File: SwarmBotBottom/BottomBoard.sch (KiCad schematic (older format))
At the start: 19 parts, among them J1 Conn_01x04_Male, J2 Conn_01x04_Male, J6 Conn_01x08_Female, U4 MCP73831-2-OT

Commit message: Camera routing with all sensors and motors
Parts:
- removed D1: LED, LED_SMD:LED_0603_1608Metric, symbol Device:LED
- removed JP1: Jumper_NO_Small, Jumper:SolderJumper-2_P1.3mm_Open_Pad1.0x1.5mm, symbol Device:Jumper_NO_Small
- removed R16, R17: R, Resistor_SMD:R_0402_1005Metric, symbol Device:R
- added C7, C8, C9: C, Capacitor_SMD:C_0402_1005Metric, symbol Device:C
- added D3: LED, LED_SMD:LED_0603_1608Metric, symbol Device:LED
- added IC1: VEML6040A3OG, VEML6040A3OG:VEML6040A3OG, symbol VEML6040A3OG:VEML6040A3OG
- added J3: Conn_01x02_Male, Connector_PinHeader_2.54mm:PinHeader_1x02_P2.54mm_Vertical_SMD_Pin1Left, symbol Connector:Conn_01x02_Male
- added R21: R, Resistor_SMD:R_0402_1005Metric, symbol Device:R
- added U3: MIC5366-3.3YC5, Package_TO_SOT_SMD:SOT-353_SC-70-5, symbol Regulator_Linear:MIC5366-3.3YC5
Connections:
- net labels added: +3.3V, SCL, SDA
- wire segments 8 -> 7
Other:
- moved on the sheet: C20, C21, D2, R15, R18, U4

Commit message: things
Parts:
- added C10: C, Capacitor_SMD:C_0402_1005Metric, symbol Device:C
- added D1, D4, D5: LED, LED_SMD:LED_0603_1608Metric, symbol Device:LED
- added IC2: PCA9570GMH, PCA9570GMH:PCA9570GMH, symbol PCA9570GMH:PCA9570GMH
- added R16, R17, R22: R, Resistor_SMD:R_0402_1005Metric, symbol Device:R
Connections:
- net +3V3: now also C10.1, IC2.8 (VDD)
- net +BATT: no longer R21.2
- net GND: now also C10.2, D1.1 (K), D4.1 (K), D5.1 (K), IC2.4 (VSS)
- net SCL: now also IC2.6 (SCL)
- net SDA: now also IC2.7 (SDA)
- new net: D4.2 (A), R17.1
- new net: D5.2 (A), R22.1
- new net: D1.2 (A), R16.1
- new net IRLED: IC2.5 (P3), R16.2
- new net POWERLED: IC2.2 (P1), R17.2
- new net UVLED: IC2.3 (P2), R22.2
- new net WHITELED: IC2.1 (P0), R21.2
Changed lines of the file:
@@
-$EndComp
-$Comp
-L power:+BATT #PWR0141
-U 1 1 5DF974D8
-P 9700 3400
-F 0 "#PWR0141" H 9700 3250 50  0001 C CNN
-F 1 "+BATT" V 9715 3527 50  0000 L CNN
-F 2 "" H 9700 3400 50  0001 C CNN
-F 3 "" H 9700 3400 50  0001 C CNN
-	1    9700 3400
-	0    -1   -1   0
 $EndComp
 $Comp
@@
 Wire Wire Line
 	700  6900 700  7300
+$Comp
+L PCA9570GMH:PCA9570GMH IC2
+U 1 1 5DFDA85C
+P 7750 5150
+F 0 "IC2" H 8250 5415 50  0000 C CNN
+F 1 "PCA9570GMH" H 8250 5324 50  0000 C CNN
+F 2 "PCA9570GMH:PCA9570GMH" H 8600 5250 50  0001 L CNN
+F 3 "https://www.nxp.com/docs/en/data-sheet/PCA9570.pdf" H 8600 5150 50  0001 L CNN
+F 4 "NXP - PCA9570GMH - I/O EXPANDER, 4BIT, 400KHZ, XQFN-8" H 8600 5050 50  0001 L CNN "Description"
+F 5 "" H 8600 4950 50  0001 L CNN "Height"
+F 6 "Nexperia" H 8600 4850 50  0001 L CNN "Manufacturer_Name"
+F 7 "PCA9570GMH" H 8600 4750 50  0001 L CNN "Manufacturer_Part_Number"
+F 8 "771-PCA9570GMH" H 8600 4650 50  0001 L CNN "Mouser Part Number"
+F 9 "https://www.mouser.com/Search/Refine.aspx?Keyword=771-PCA9570GMH" H 8600 4550 50  0001 L CNN "Mouser Price/Stock"
+F 10 "" H 8600 4450 50  0001 L CNN "RS Part Number"
+F 11 "" H 8600 4350 50  0001 L CNN "RS Price/Stock"
+	1    7750 5150
+	1    0    0    -1
+$EndComp
+Text Label 8750 5350 0    50   ~ 0
+SDA
+Text Label 8750 5250 0    50   ~ 0
+SCL
+$Comp
+L power:GND #PWR0141
+U 1 1 5DFDB907
+P 7750 5450
+F 0 "#PWR0141" H 7750 5200 50  0001 C CNN
+F 1 "GND" V 7755 5322 50  0000 R CNN
+F 2 "" H 7750 5450 50  0001 C CNN
+F 3 "" H 7750 5450 50  0001 C CNN
+	1    7750 5450
+	0    1    1    0
+$EndComp
+$Comp
+L Device:C C10
+U 1 1 5DFDBAA0
+P 8750 5600
+F 0 "C10" H 8865 5646 50  0000 L CNN
+F 1 "C" H 8865 5555 50  0000 L CNN
+F 2 "Capacitor_SMD:C_0402_1005Metric" H 8788 5450 50  0001 C CNN
+F 3 "~" H 8750 5600 50  0001 C CNN
+	1    8750 5600
+	1    0    0    -1
+$EndComp
+$Comp
+L power:+3.3V #PWR0143
+U 1 1 5DFDBDF8
+P 8750 5450
+F 0 "#PWR0143" H 8750 5300 50  0001 C CNN
+F 1 "+3.3V" V 8765 5578 50  0000 L CNN
+F 2 "" H 8750 5450 50  0001 C CNN
+F 3 "" H 8750 5450 50  0001 C CNN
+	1    8750 5450
+	0    1    1    0
+$EndComp
+Connection ~ 8750 5450
+$Comp
+L power:GND #PWR0144
+U 1 1 5DFDC25F
+P 8750 5750
+F 0 "#PWR0144" H 8750 5500 50  0001 C CNN
+F 1 "GND" H 8755 5577 50  0000 C CNN
+F 2 "" H 8750 5750 50  0001 C CNN
+F 3 "" H 8750 5750 50  0001 C CNN
+	1    8750 5750
+	1    0    0    -1
+$EndComp
+$Comp
+L Device:LED D4
+U 1 1 5DFDE198
+P 10200 4550
+F 0 "D4" H 10193 4295 50  0000 C CNN
+F 1 "LED" H 10193 4386 50  0000 C CNN
+F 2 "LED_SMD:LED_0603_1608Metric" H 10200 4550 50  0001 C CNN
+F 3 "~" H 10200 4550 50  0001 C CNN
+	1    10200 4550
+	-1   0    0    1
+$EndComp
+$Comp
+L Device:R R17
+U 1 1 5DFDE19E
+P 9900 4550
+F 0 "R17" V 9693 4550 50  0000 C CNN
+F 1 "R" V 9784 4550 50  0000 C CNN
+F 2 "Resistor_SMD:R_0402_1005Metric" V 9830 4550 50  0001 C CNN
+F 3 "~" H 9900 4550 50  0001 C CNN
+	1    9900 4550
+	0    1    1    0
+$EndComp
+$Comp
+L power:GND #PWR0145
+U 1 1 5DFDE1AA
+P 10350 4550
+F 0 "#PWR0145" H 10350 4300 50  0001 C CNN
+F 1 "GND" H 10355 4377 50  0000 C CNN
+F 2 "" H 10350 4550 50  0001 C CNN
+F 3 "" H 10350 4550 50  0001 C CNN
+	1    10350 4550
+	1    0    0    -1
+$EndComp
+$Comp
+L Device:LED D5
+U 1 1 5DFDE8F2
+P 10200 5050
+F 0 "D5" H 10193 4795 50  0000 C CNN
+F 1 "LED" H 10193 4886 50  0000 C CNN
+F 2 "LED_SMD:LED_0603_1608Metric" H 10200 5050 50  0001 C CNN
+F 3 "~" H 10200 5050 50  0001 C CNN
+	1    10200 5050
+	-1   0    0    1
+$EndComp
+$Comp
+L Device:R R22
+U 1 1 5DFDE8F8
+P 9900 5050
+F 0 "R22" V 9693 5050 50  0000 C CNN
+F 1 "R" V 9784 5050 50  0000 C CNN
+F 2 "Resistor_SMD:R_0402_1005Metric" V 9830 5050 50  0001 C CNN
+F 3 "~" H 9900 5050 50  0001 C CNN
+	1    9900 5050
+	0    1    1    0
+$EndComp
+$Comp
+L power:GND #PWR0146
+U 1 1 5DFDE904
+P 10350 5050
+F 0 "#PWR0146" H 10350 4800 50  0001 C CNN
+F 1 "GND" H 10355 4877 50  0000 C CNN
+F 2 "" H 10350 5050 50  0001 C CNN
+F 3 "" H 10350 5050 50  0001 C CNN
+	1    10350 5050
+	1    0    0    -1
+$EndComp
+$Comp
+L Device:LED D1
+U 1 1 5DFDF294
+P 10150 5550
+F 0 "D1" H 10143 5295 50  0000 C CNN
+F 1 "LED" H 10143 5386 50  0000 C CNN
+F 2 "LED_SMD:LED_0603_1608Metric" H 10150 5550 50  0001 C CNN
+F 3 "~" H 10150 5550 50  0001 C CNN
+	1    10150 5550
+	-1   0    0    1
+$EndComp
+$Comp
+L Device:R R16
+U 1 1 5DFDF29A
+P 9850 5550
+F 0 "R16" V 9643 5550 50  0000 C CNN
+F 1 "R" V 9734 5550 50  0000 C CNN
+F 2 "Resistor_SMD:R_0402_1005Metric" V 9780 5550 50  0001 C CNN
+F 3 "~" H 9850 5550 50  0001 C CNN
+	1    9850 5550
+	0    1    1    0
+$EndComp
+$Comp
+L power:GND #PWR0147
+U 1 1 5DFDF2A6
+P 10300 5550
+F 0 "#PWR0147" H 10300 5300 50  0001 C CNN
+F 1 "GND" H 10305 5377 50  0000 C CNN
+F 2 "" H 10300 5550 50  0001 C CNN
+F 3 "" H 10300 5550 50  0001 C CNN
+	1    10300 5550
+	1    0    0    -1
+$EndComp
+Text Label 7750 5150 2    50   ~ 0
+WHITELED
+Text Label 7750 5250 2    50   ~ 0
+POWERLED
+Text Label 7750 5350 2    50   ~ 0
+UVLED
+Text Label 8750 5150 0    50   ~ 0
+IRLED
+Text Label 9700 5550 2    50   ~ 0
+IRLED
+Text Label 9750 5050 2    50   ~ 0
+UVLED
+Text Label 9750 4550 2    50   ~ 0
+POWERLED
+Text Label 9700 3400 2    50   ~ 0
+WHITELED
 $EndSCHEMATC

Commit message: Final Design
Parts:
- removed D3: LED, LED_SMD:LED_0603_1608Metric, symbol Device:LED
- removed IC2: PCA9570GMH, PCA9570GMH:PCA9570GMH, symbol PCA9570GMH:PCA9570GMH
- removed R21: R, Resistor_SMD:R_0402_1005Metric, symbol Device:R
- added C11: 10uF, Capacitor_SMD:C_0402_1005Metric, symbol Device:C
- added C12: 0.1uF, Capacitor_SMD:C_0402_1005Metric, symbol Device:C
- added IC2: PCA9532BS,118, Package_DFN_QFN:VQFN-24-1EP_4x4mm_P0.5mm_EP2.45x2.45mm, symbol PCA9532BS_118:PCA9532BS,118
- added IC3: VEML6040A3OG, VEML6040A3OG:VEML6040A3OG, symbol VEML6040A3OG:VEML6040A3OG
- added U5: TCA9548AMRGER, Package_DFN_QFN:Texas_RGE0024C_EP2.1x2.1mm, symbol Interface_Expansion:TCA9548AMRGER
- C10, C7: value C -> 0.1uF
- C20, C21, C8, C9: value C -> 1uF
- D1, D2, D4: value LED -> WHITE
- D5: value LED -> UV
- J1, J2: footprint Connector_PinSocket_2.54mm:PinSocket_1x04_P2.54mm_Vertical_SMD_Pin1Left -> Connector_PinSocket_2.54mm:PinSocket_1x04_P2.54mm_Vertical_SMD_Pin1Right
- J3: footprint Connector_PinHeader_2.54mm:PinHeader_1x02_P2.54mm_Vertical_SMD_Pin1Left -> Connector_PinHeader_2.54mm:PinHeader_1x02_P2.54mm_Vertical_SMD_Pin1Right
- R15, R18: value R -> 470R
- R16, R17, R22: value R -> 330R
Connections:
- net +3V3: now also C10.2, C11.2, C12.1, IC2.21, IC2.22, IC2.23, IC3.4 (VDD), U5.21 (VCC), U5.24 (~RESET); no longer C10.1
- net GND: now also C10.1, C11.1, C12.2, IC2.24, IC2.25, IC3.1 (GND), U5.18 (A2), U5.22 (A0), U5.23 (A1), U5.9 (GND); no longer C10.2
- net IRLED: now also IC2.1
- net POWERLED: now also IC2.3
- net SCL: now also IC2.19, U5.19 (SCL); no longer IC1.3 (SCLK)
- net SDA: now also IC2.20, U5.20 (SDA); no longer IC1.2 (SDAT)
- net UVLED: now also IC2.2
- new net CURRSETL: IC2.6
- new net CURRSETR: IC2.16
- new net SCL1: IC1.3 (SCLK), U5.15 (SC6)
- new net SCL2: IC3.3 (SCLK), U5.6 (SC2)
- new net SDA1: IC1.2 (SDAT), U5.14 (SD6)
- new net SDA2: IC3.2 (SDAT), U5.5 (SD2)
- new net STEPPERENL: IC2.5
- new net STEPPERENR: IC2.17
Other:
- moved on the sheet: C10, C7, C8, C9, U3

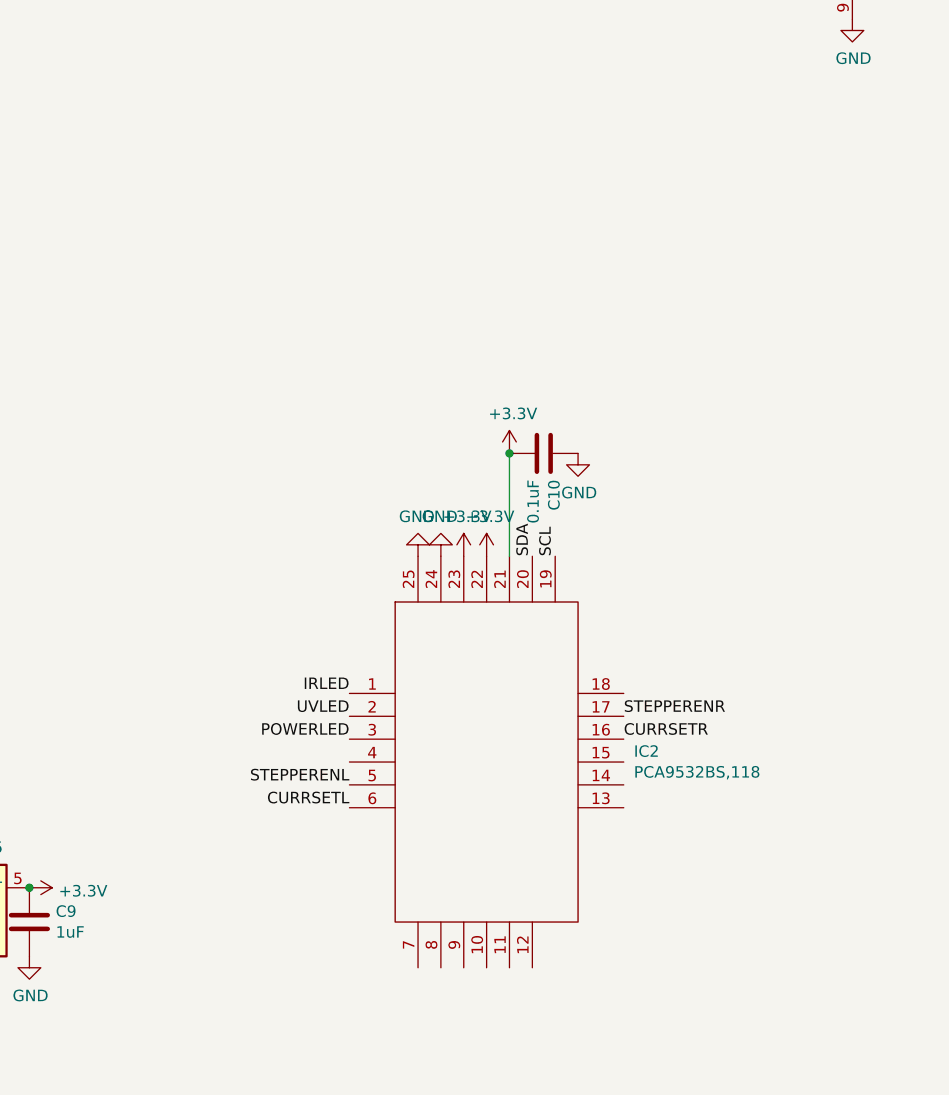
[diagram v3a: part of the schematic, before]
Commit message: Updated LED drivers
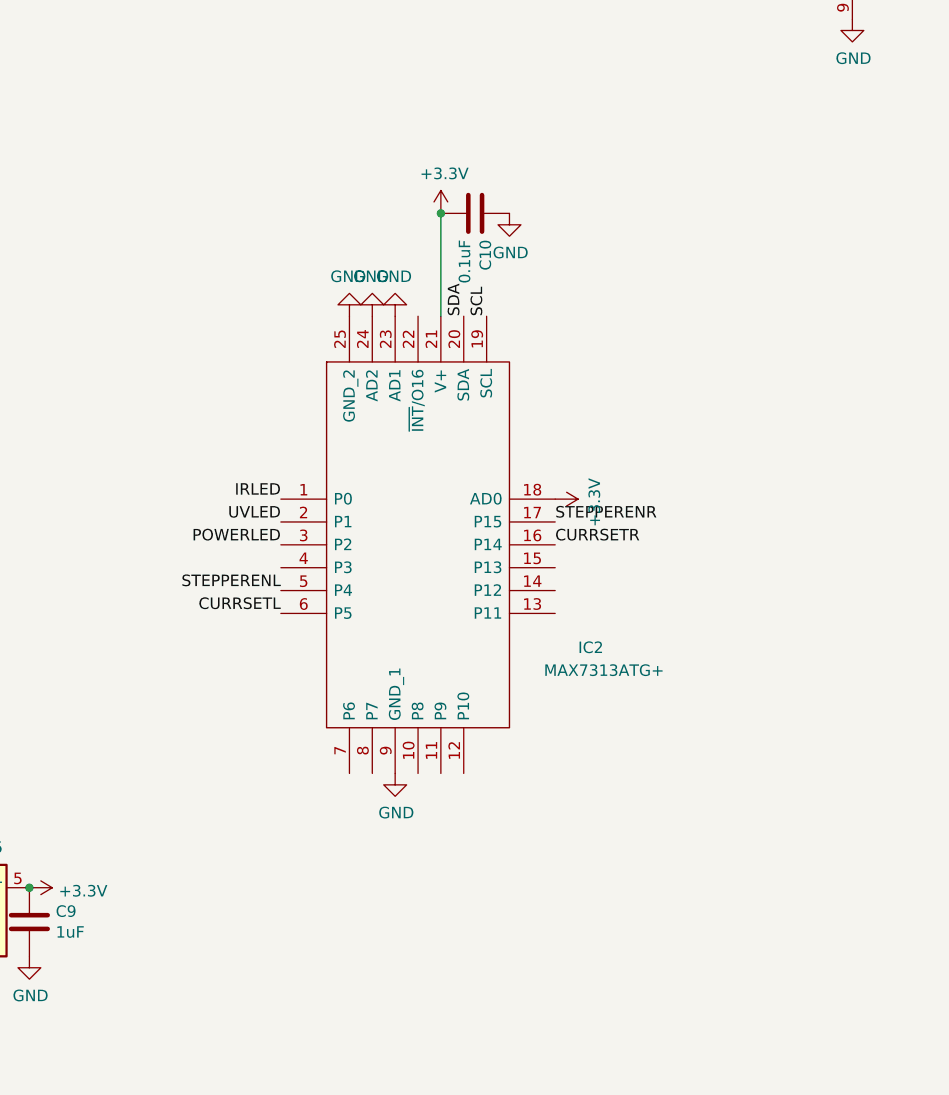
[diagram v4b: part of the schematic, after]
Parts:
- removed IC2: PCA9532BS,118, Package_DFN_QFN:VQFN-24-1EP_4x4mm_P0.5mm_EP2.45x2.45mm, symbol PCA9532BS_118:PCA9532BS,118
- added IC2: MAX7313ATG+, MAX7313ATG+:QFN50P400X400X80-25N, symbol MAX7313ATG+:MAX7313ATG+
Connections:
- net +3V3: now also IC2.18 (AD0), IC2.21 (V+)
- net CURRSETL: now also IC2.6 (P5)
- net CURRSETR: now also IC2.16 (P14)
- net GND: now also IC2.23 (AD1), IC2.24 (AD2), IC2.25 (GND_2), IC2.9 (GND_1)
- net IRLED: now also IC2.1 (P0)
- net POWERLED: now also IC2.3 (P2)
- net SCL: now also IC2.19 (SCL)
- net SDA: now also IC2.20 (SDA)
- net STEPPERENL: now also IC2.5 (P4)
- net STEPPERENR: now also IC2.17 (P15)
- net UVLED: now also IC2.2 (P1)
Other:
- moved on the sheet: C10
